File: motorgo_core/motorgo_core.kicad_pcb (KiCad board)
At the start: 4 copper layers, 65 x 56 mm, 137 parts, among them J1 USB4520-03-0-A_REVA, J12 Conn_01x04_Pin, J13 I2C_STANDARDQWIIC, J15 I2C_STANDARDQWIIC, J16 BM05B-SRSS-TB_LF__SN_, J18 BM05B-SRSS-TB_LF__SN_, J4 Conn_02x20_Odd_Even, J5 Conn_01x04_Pin, J6 DNP, J7 Conn_02x20_Odd_Even, J8 DNP, J9 Conn_01x04_Pin, Q1 AP30H80Q, Q10 AP30H80Q, Q11 AP30H80Q, Q12 AP30H80Q, Q2 AP30H80Q, Q3 AP30H80Q, Q4 AP30H80Q, Q5 AP30H80Q, Q6 AP30H80Q, Q7 AP30H80Q, Q8 AP30H80Q, Q9 AP30H80Q, U1 ESP32-S3-WROOM-1, U10 LIS3MDLTR, U11 LSM6DS3TR, U2 USBLC6-2P6, U3 FD6288, U4 FD6288, U6 TPS54620RHLR, U8 AMS1117-3.3

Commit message: update to recent production
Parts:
- removed kibuzzard-670F41F1: G***, kibuzzard-670F41F1
- removed kibuzzard-67320F82: G***, kibuzzard-67320F82
- removed kibuzzard-67320F9F: G***, kibuzzard-67320F9F
- added kibuzzard-6740A353: G***, kibuzzard-6740A353, F.Cu at (146.8, 88.3)
- added kibuzzard-6740A48B: G***, kibuzzard-6740A48B, F.Cu at (169.3, 99.6)
- added kibuzzard-6740A543: G***, kibuzzard-6740A543, F.Cu at (166.6, 81.0)
- added kibuzzard-6740A668: G***, kibuzzard-6740A668, F.Cu at (120.6, 112.0)
- added kibuzzard-6740A668: G***, kibuzzard-6740A668, F.Cu at (125.6, 112.0)
- added kibuzzard-6740A681: G***, kibuzzard-6740A681, F.Cu at (143.5, 111.9)
- added kibuzzard-6740A681: G***, kibuzzard-6740A681, F.Cu at (148.6, 111.9)
- added kibuzzard-6740AFFF: G***, kibuzzard-6740AFFF, B.Cu at (153.2, 71.9)
- added kibuzzard-6740B00B: G***, kibuzzard-6740B00B, B.Cu at (152.6, 74.7)
- added kibuzzard-6740B03C: G***, kibuzzard-6740B03C, B.Cu at (161.2, 76.9)
- added kibuzzard-6740B0CA: G***, kibuzzard-6740B0CA, F.Cu at (164.4, 81.2)
- added kibuzzard-6740B1FD: G***, kibuzzard-6740B1FD, F.Cu at (167.8, 72.3)
- added kibuzzard-6740B20C: G***, kibuzzard-6740B20C, F.Cu at (167.8, 69.2)
- added kibuzzard-6740E9DD: G***, kibuzzard-6740E9DD, B.Cu at (134.8, 73.0)
- added kibuzzard-6740EACA: G***, kibuzzard-6740EACA, B.Cu at (149.0, 81.5)
- C1: value 68pf -> 68pf 10v
- C15, C2: value 4.7uF 1mOhm -> 4.7uF 1mOhm 25v
- C20: value 6.8nf -> 6.8nf 10v
- C23: value 47uF 3mOhm -> 47uF 3mOhm 25v
- C26, C30, C31, C34, C39, C4, C46, C9: value 100nF -> 100nF 10v
- C3, C33: value 100nF -> 100nF 25v
- C32: value 1uF -> 1uF 10v
- D1: value LED -> LED blue
- D10, D5, D6, D7, D8, D9: value D_Schottky -> D_Schottky C7420331
- D2: value LED -> LED green
- D3: value LED -> LED red
- J11: value ~ -> xt30
- J2, J3: value ~ -> C2886897
- L1: value 2.2uH 12.7mOhm -> 2.2uH 12.7mOhm C5440776
- moved kibuzzard-673237E1 5.11 mm to (158.3, 76.8)
- moved C32 2.20 mm to (146.2, 70.1), turned to 90 degrees
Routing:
- net GND: track 100.9 -> 103.9 mm
- net +3.3V: track 223.3 -> 221.1 mm
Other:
- outline, holes or cut-outs redrawn
- board text removed: "38 40 39 37"
- board text removed: "5V"
- board text removed: "GND"

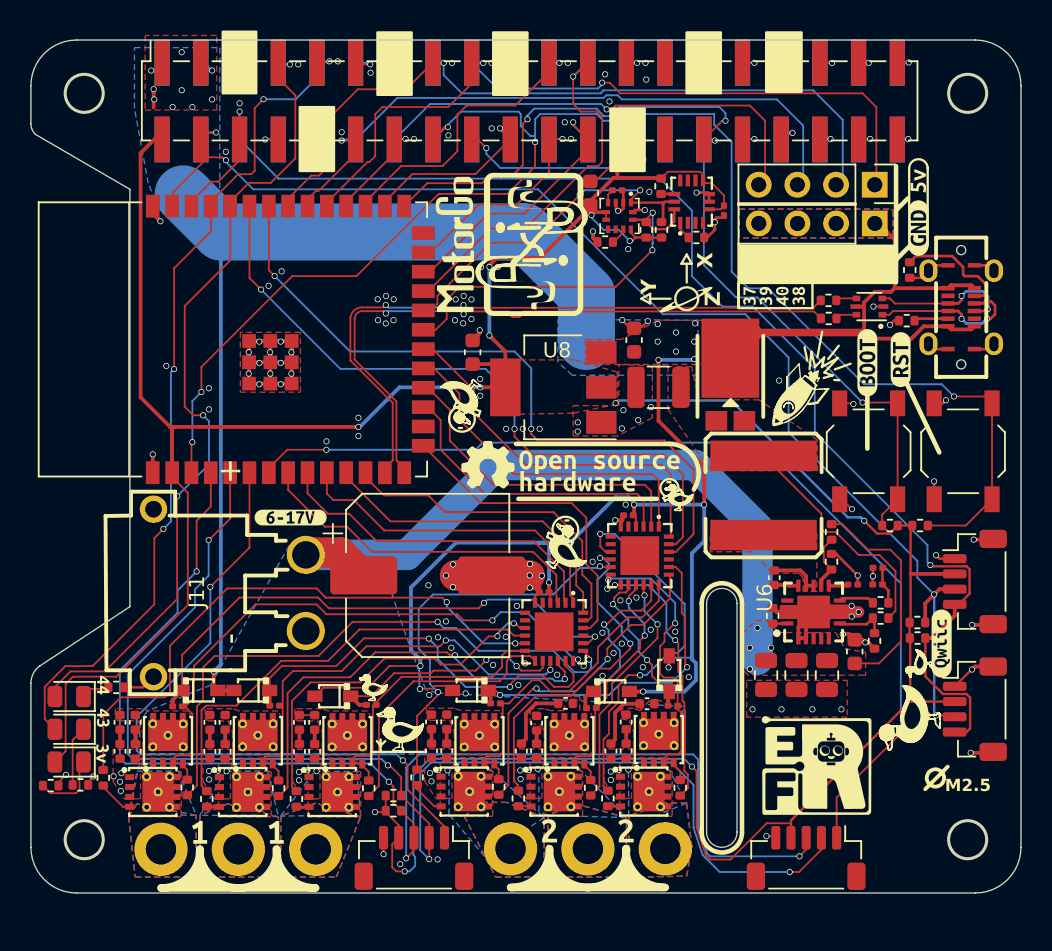
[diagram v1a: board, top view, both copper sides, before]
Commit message: fix polarity of our xt30 connector, add jumper to disconnect 3v rail from pi-header
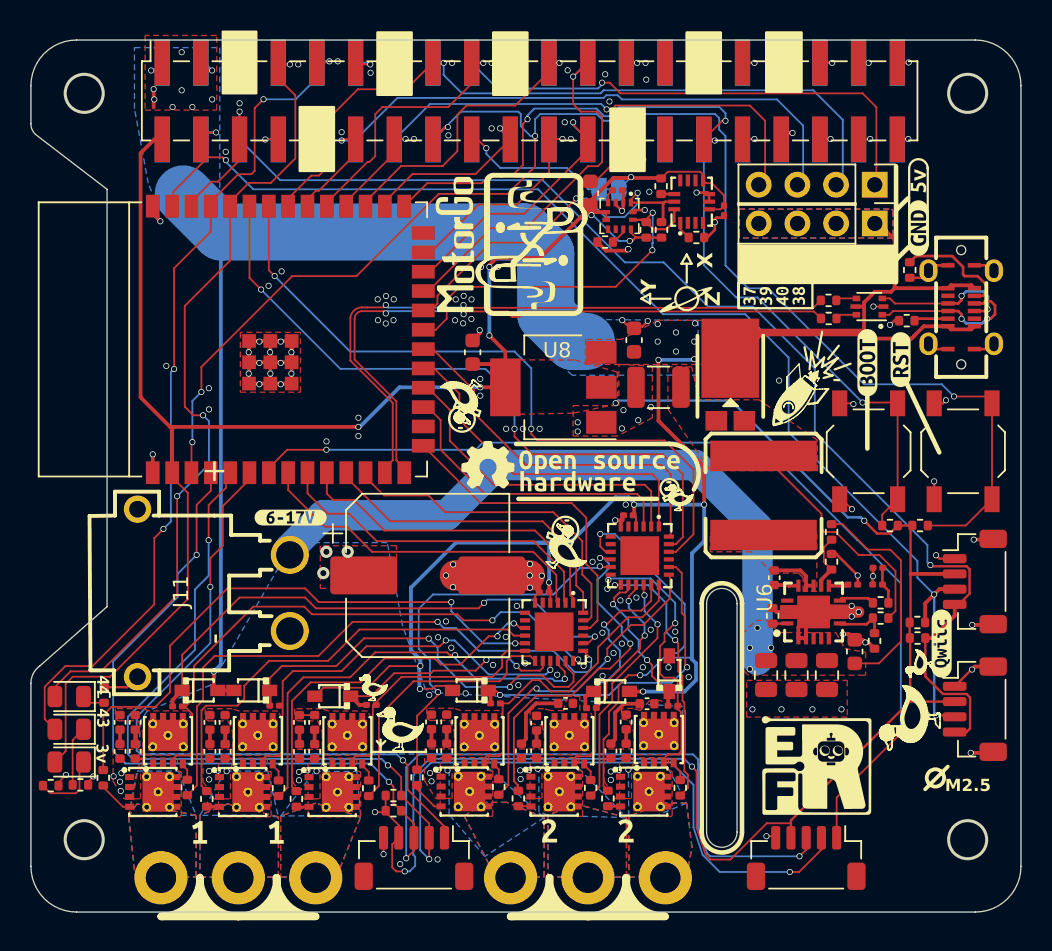
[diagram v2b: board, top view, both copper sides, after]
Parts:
- added REF**: SolderJumper-2_P1.3mm_Open_RoundedPad1.0x1.5mm, Jumper:SolderJumper-2_P1.3mm_Open_RoundedPad1.0x1.5mm, B.Cu at (147.4, 69.8)
- added kibuzzard-67A57D3F: G***, kibuzzard-67A57D3F, B.Cu at (143.5, 69.8)
- moved J8 1.90 mm to (146.1, 115.0)
- moved J6 1.87 mm to (123.1, 115.0)
- moved J11 1.05 mm to (121.5, 96.3)
- moved R1 0.94 mm to (114.3, 103.0), turned to 90 degrees
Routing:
- net +BATT: track 62.5 -> 15.5 mm, vias 4 -> 3
- net GND: track 103.9 -> 149.3 mm, vias 171 -> 174
- net scl: track 89.9 -> 87.3 mm
- net +3.3V: track 221.1 -> 222.9 mm
- net /i2c_1.scl: track 23.6 -> 24.5 mm
- net +5V: track 177.7 -> 178.2 mm
- net Net-(U3-LO2): track 29.1 -> 29.6 mm
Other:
- board size 65 x 56 mm -> 65 x 57.2 mm
